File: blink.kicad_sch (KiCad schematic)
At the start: 9 parts, among them J1 ICSP, SW1 RESET, U1 ATmega328-P, Y1 18.432 MHz

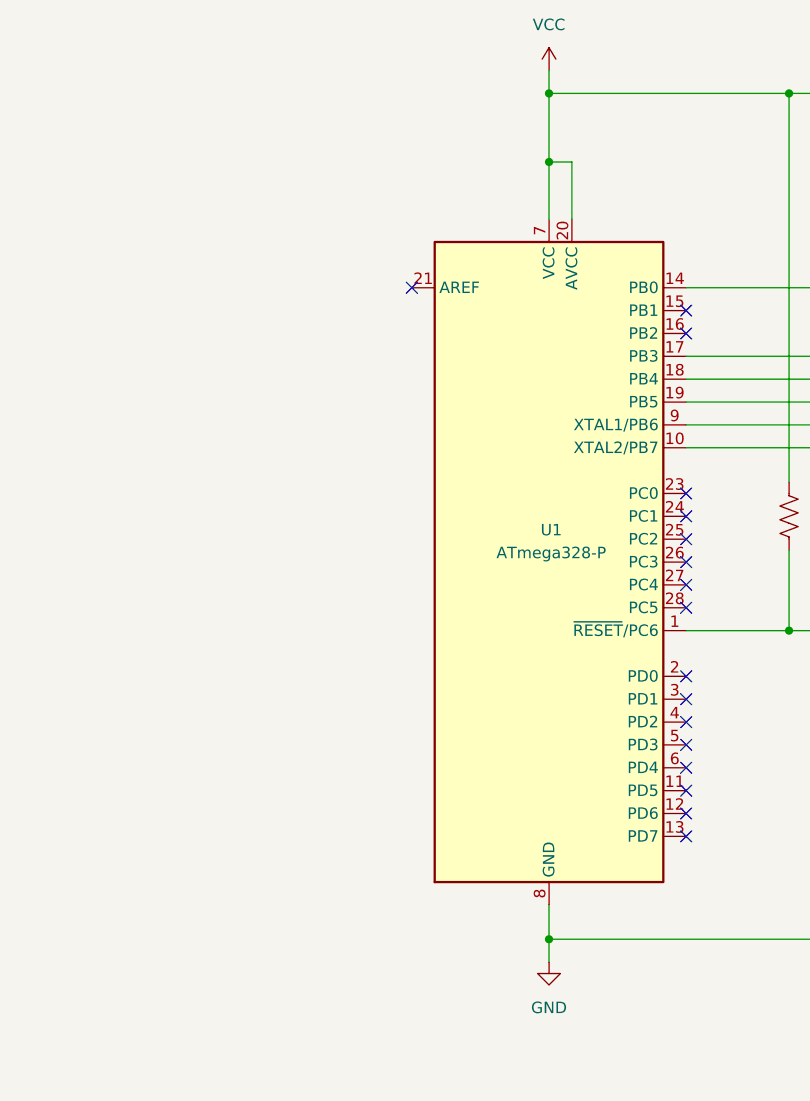
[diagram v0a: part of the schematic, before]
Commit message: add decoupling cap
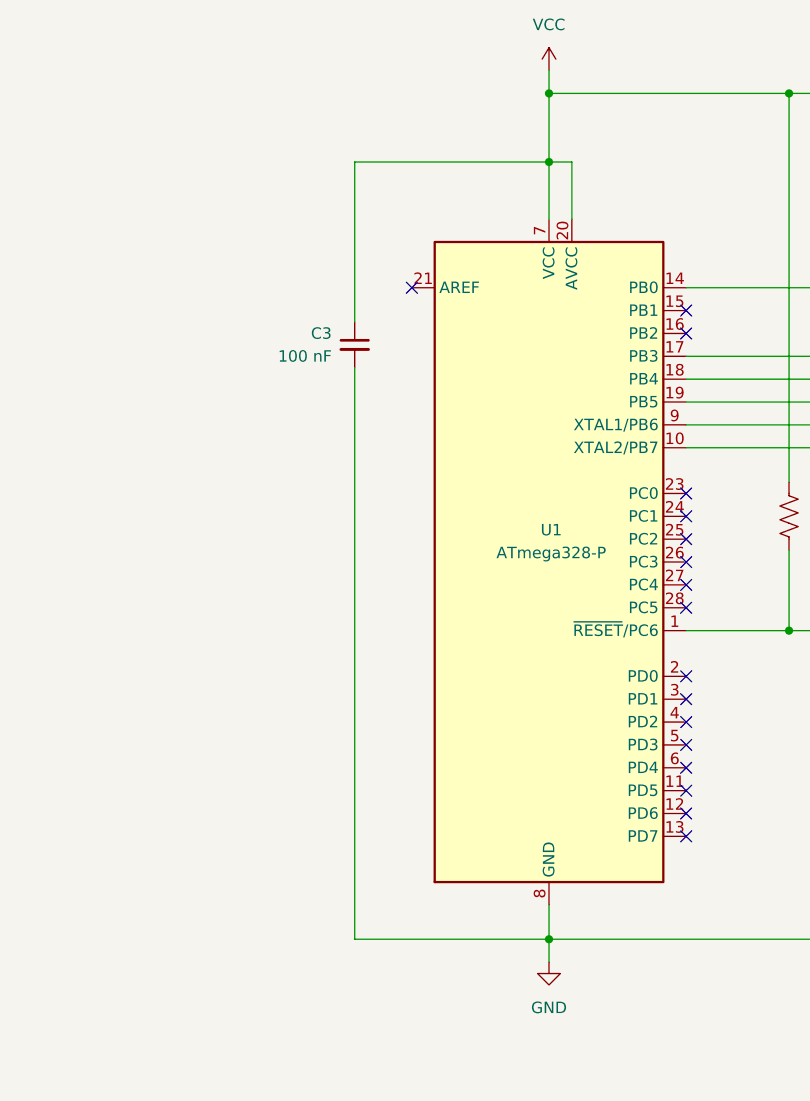
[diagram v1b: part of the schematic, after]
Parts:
- added C3: 100 nF, symbol Device:C_Small
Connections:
- net GND: now also C3.2
- net VCC: now also C3.1
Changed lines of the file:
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@@
+	(wire
+		(pts
+			(xy 74.93 139.7) (xy 96.52 139.7)
+		)
+		(stroke
+			(width 0)
+			(type default)
+		)
+	)
 	(wire
 		(pts
@@
 	(wire
 		(pts
+			(xy 74.93 76.2) (xy 74.93 139.7)
+		)
+		(stroke
+			(width 0)
+			(type default)
+		)
+	)
+	(wire
+		(pts
 			(xy 133.35 105.41) (xy 123.19 105.41)
 		)
@@
 	(wire
 		(pts
+			(xy 96.52 53.34) (xy 74.93 53.34)
+		)
+		(stroke
+			(width 0)
+			(type default)
+		)
+	)
+	(wire
+		(pts
 			(xy 195.58 81.28) (xy 195.58 87.63)
 		)
@@
 		(pts
 			(xy 96.52 43.18) (xy 96.52 45.72)
+		)
+		(stroke
+			(width 0)
+			(type default)
+		)
+	)
+	(wire
+		(pts
+			(xy 74.93 53.34) (xy 74.93 71.12)
 		)
 		(stroke
@@
 					(unit 1)
 				)
+			)
+		)
+	)
+	(symbol
+		(lib_id "Device:C_Small")
+		(at 74.93 73.66 0)
+		(mirror y)
+		(unit 1)
+		(exclude_from_sim no)
+		(in_bom yes)
+		(on_board yes)
+		(dnp no)
+		(property "Reference" "C3"
+			(at 72.39 72.3962 0)
+			(effects
+				(font
+					(size 1.27 1.27)
+				)
+				(justify left)
+			)
+		)
+		(property "Value" "100 nF"
+			(at 72.39 74.9362 0)
+			(effects
+				(font
+					(size 1.27 1.27)
+				)
+				(justify left)
+			)
+		)
+		(property "Footprint" ""
+			(at 74.93 73.66 0)
+			(effects
+				(font
+					(size 1.27 1.27)
+				)
+				(hide yes)
+			)
+		)
+		(property "Datasheet" "~"
+			(at 74.93 73.66 0)
+			(effects
+				(font
+					(size 1.27 1.27)
+				)
+				(hide yes)
+			)
+		)
+		(property "Description" "Unpolarized capacitor, small symbol"
+			(at 74.93 73.66 0)
+			(effects
+				(font
+					(size 1.27 1.27)
+				)
+				(hide yes)
+			)
+		)
+		(pin "2"
+		)
+		(pin "1"
+		)
+		(instances
+			(project ""
+				(path "/69937047-ac34-43c6-88b3-07ef58062bfb"
+					(reference "C3")
+					(unit 1)
+				)
